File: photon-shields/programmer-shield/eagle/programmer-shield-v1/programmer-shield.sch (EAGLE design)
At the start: 57 parts, among them IC1 FT2232HQLQFP, IC2 AT93C46A-10TQ-2.7, IC3 LM1117IMPX-3.3, Q1 MPSA42, Y1 12MHZ

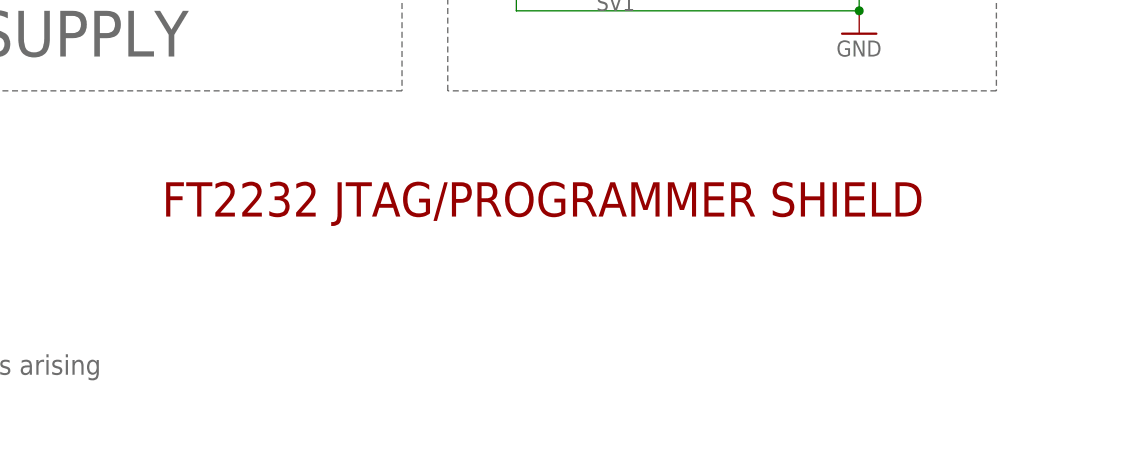
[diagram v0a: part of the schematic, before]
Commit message: added rev numbers to schematic sheets and regenerated the PDFs
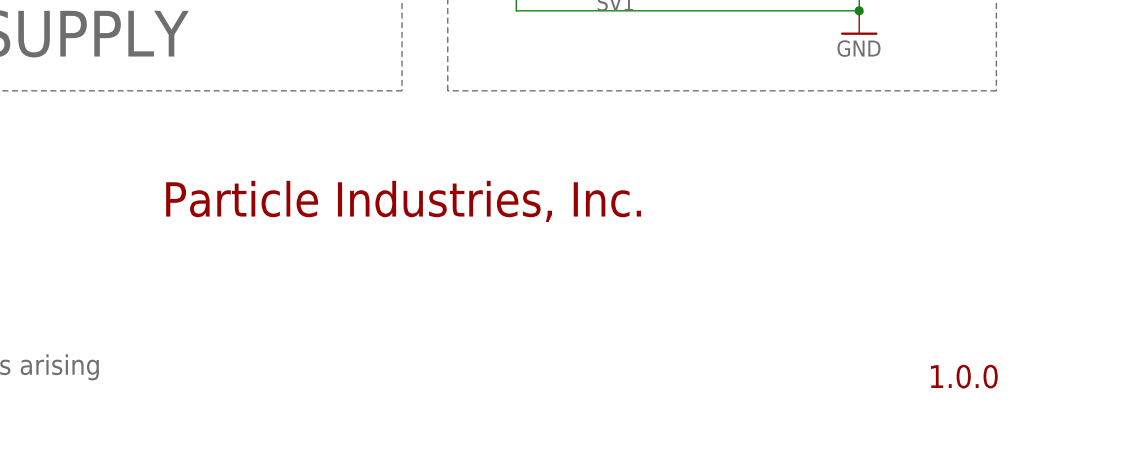
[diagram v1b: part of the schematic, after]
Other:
- note added: "1.0.0"
- note added: "Particle Industries, Inc."
- note removed: "FT2232 JTAG/PROGRAMMER SHIELD"
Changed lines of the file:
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@@
 <setting verticaltext="up"/>
 </settings>
-<grid distance="0.05" unitdist="inch" unit="inch" style="lines" multiple="1" display="yes" altdistance="0.01" altunitdist="inch" altunit="inch"/>
+<grid distance="0.1" unitdist="inch" unit="inch" style="lines" multiple="1" display="no" altdistance="0.01" altunitdist="inch" altunit="inch"/>
 <layers>
 <layer number="1" name="Top" color="4" fill="1" visible="no" active="no"/>
@@
 <sheet>
 <plain>
-<text x="290.83" y="26.67" size="3.81" layer="94">FT2232 JTAG/PROGRAMMER SHIELD</text>
+<text x="290.83" y="26.67" size="3.81" layer="94">Particle Industries, Inc.</text>
 <wire x1="5.08" y1="40.64" x2="236.22" y2="40.64" width="0.1524" layer="95" style="dashdot"/>
 <wire x1="236.22" y1="40.64" x2="236.22" y2="259.08" width="0.1524" layer="95" style="dashdot"/>
@@
 from future changes to them. The product information on the Web Site or Materials is subject to change without notice. Do not finalize a design with this information.
 Particle is a registered trademark.</text>
+<text x="375.92" y="7.62" size="2.54" layer="94">1.0.0</text>
 </plain>
 <instances>
